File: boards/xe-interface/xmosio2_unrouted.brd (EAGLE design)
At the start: 116.8 x 55.2 mm, 105 parts, among them IC1 IDTQS3245QSOP20, IC2 IDTQS3245QSOP20, IC3 IDTQS3245QSOP20, IC4 IDTQS3245QSOP20, IC5 IDTQS3245QSOP20, U1 24 MHz Osc. (F535L-24), X1 0446200002

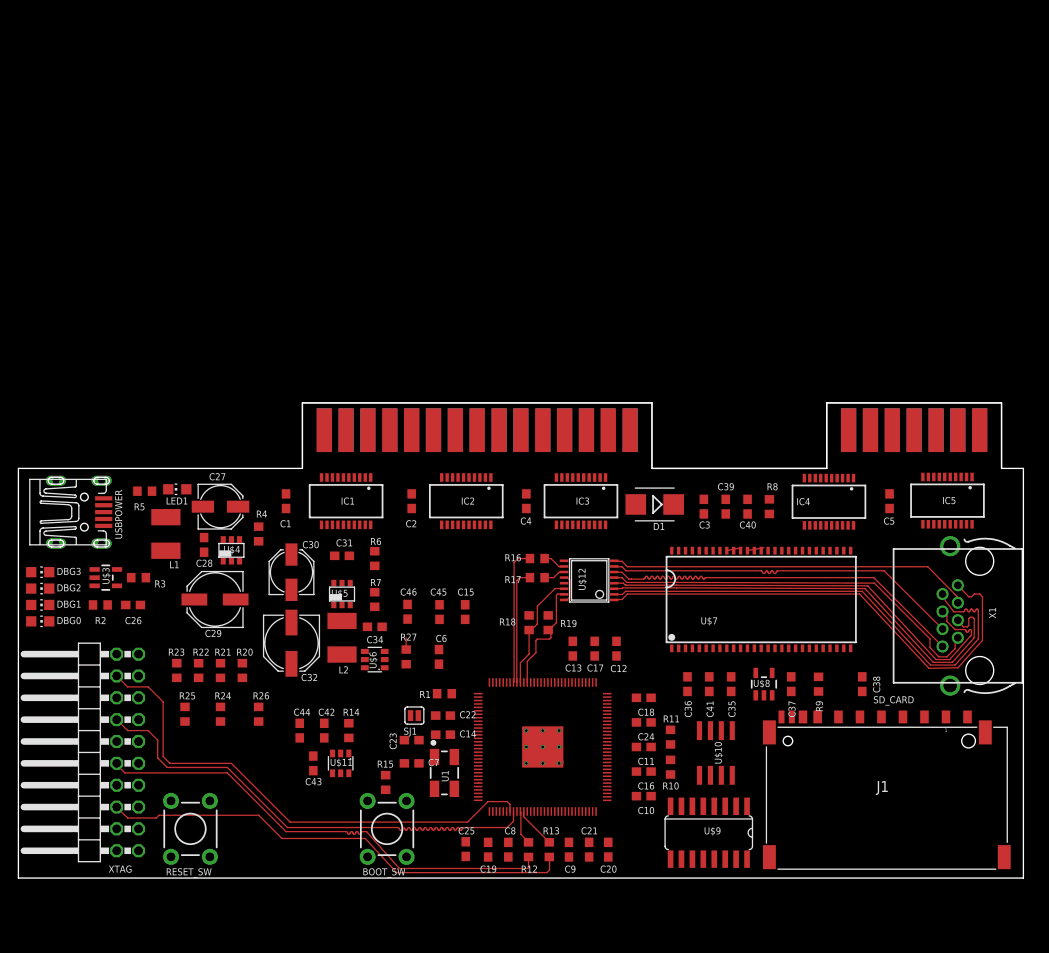
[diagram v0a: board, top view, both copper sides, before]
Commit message: Save the currently-unrouted-apart-from-high-speed-traces board in case something goes wrong
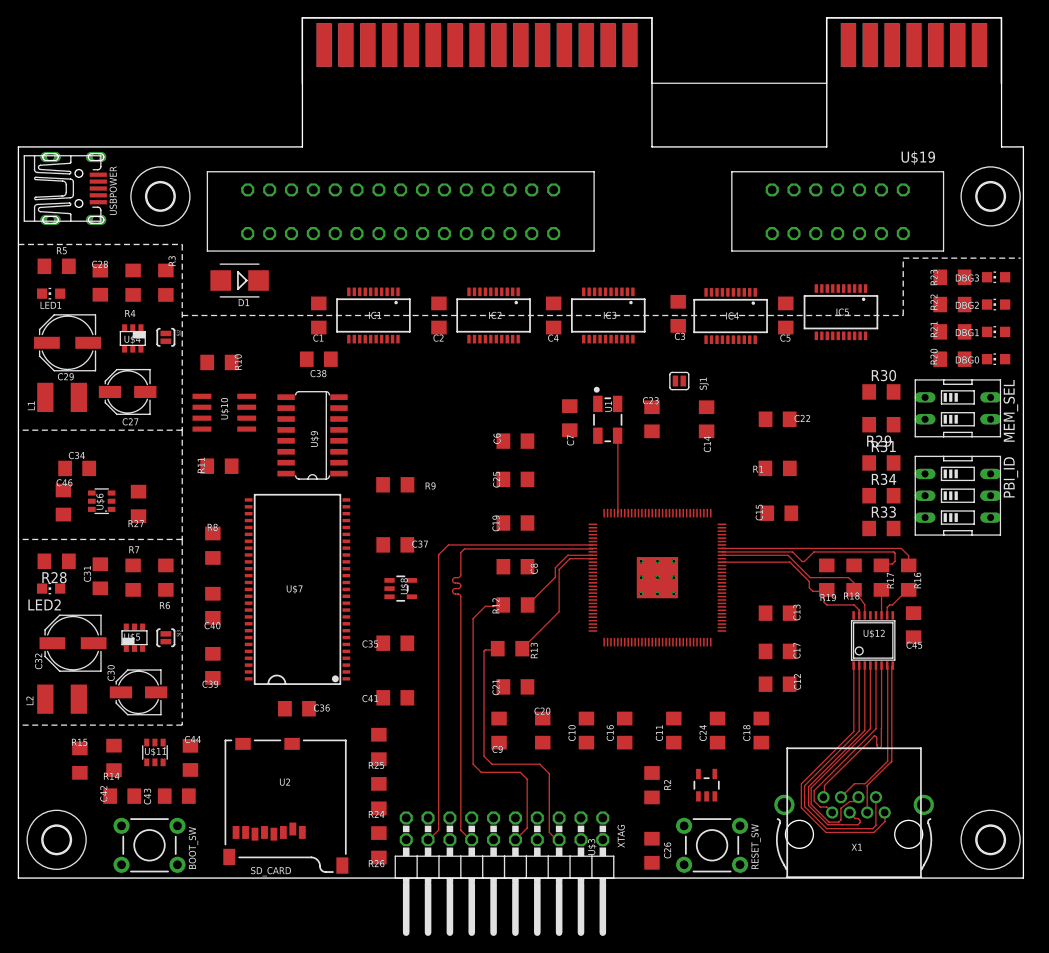
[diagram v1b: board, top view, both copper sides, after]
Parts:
- removed J1: (no value), InputOutputIO (rev17e):693063020911
- added H1, H2, H3, H4: MOUNT-HOLE3.2, holes:3,2
- added LED2: ok33, led:CHIP-LED0805
- added MEM_SEL: (no value), special:EDG-02
- added PBI_ID: (no value), special:EDG-03
- added R28: 47R, rcl:R1206
- added R29, R30, R31, R33, R34: 10K, rcl:R1206
- added SJ2, SJ3: SOLDERJUMPERNO, SparkFun:SJ_2S-NO
- added U$19: XE_SLOT, pbxl:XE_SLOT
- added U2: USD-SOCKETNEW, SparkFun-Connectors:MICRO-SD-SOCKET-PP
- C1, C10, C11, C12, C13, C14, C15, C16, C17, C18, C19, C2, C20, C21, C22, C23, C24, C25, C26, C28, C3, C31, C34, C35, C36, C37, C38, C39, C4, C40, C41, C42, C43, C44, C45, C46, C5, C6, C7, C8, C9: device rcl:C0603 -> rcl:C1206
- R1, R10, R11, R12, R13, R14, R15, R16, R17, R18, R19, R2, R20, R21, R22, R23, R24, R25, R26, R27, R3, R4, R5, R6, R7, R8, R9: device rcl:R0603 -> rcl:R1206
- moved DBG3 116.3 mm to (113.7, 69.8), turned to 90 degrees
- moved DBG2 115.9 mm to (113.7, 66.7), turned to 90 degrees
- moved DBG1 115.6 mm to (113.7, 63.5), turned to 90 degrees
- moved DBG0 115.2 mm to (113.7, 60.3), turned to 90 degrees
- moved R23 101.1 mm to (108.6, 69.8), turned to 180 degrees
- moved R22 97.4 mm to (108.6, 66.7), turned to 180 degrees
- moved R21 93.8 mm to (108.6, 63.5), turned to 180 degrees
- moved R20 90.1 mm to (108.6, 60.3), turned to 180 degrees
- moved U$3 73.9 mm to (80.0, 10.8), turned to 0 degrees
- moved C38 73.6 mm to (34.9, 60.3), turned to 180 degrees
- moved R10 70.5 mm to (23.4, 59.9), turned to 0 degrees
- moved U$10 69.5 mm to (23.9, 54.1), turned to 90 degrees
- moved R2 67.5 mm to (73.7, 10.8), turned to 90 degrees
- moved C26 66.8 mm to (73.7, 3.17), turned to 270 degrees
- moved U$9 65.2 mm to (34.2, 51.5), turned to 90 degrees
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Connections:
- removed net N$40: J1.CD
- removed net N$41: J1.WP
- new net N$30: C29.+, L1.1, LED1.A, R3.2, SJ2.1
- new net N$31: LED2.C, R28.2
- new net N$32: C32.+, L2.1, LED2.A, R6.2, SJ3.1
- new net N$34: MEM_SEL.2, R29.1, U$2.25
- new net N$35: MEM_SEL.1, R30.2, U$2.26
- new net PBI0: PBI_ID.1, R31.2, U$2.33
- new net PBI1: PBI_ID.2, R34.2, U$2.61
- new net PBI2: PBI_ID.3, R33.2, U$2.62
- net +5V: now also U$19.26, U$19.44
- net B1: now also U$19.1
- net B10: now also U$19.11
- net B11: now also U$19.12
- net B12: now also U$19.13
- net B13: now also U$19.14
- net B14: now also U$19.15
- net B15: now also U$19.16
- net B16: now also U$19.17
- net B17: now also U$19.18
- net B18: now also U$19.19
- net B19: now also U$19.20
- net B2: now also U$19.2
- net B20: now also U$19.21
- net B21: now also U$19.22
- net B22: now also U$19.23
- net B23: now also U$19.24
- net B24: now also U$19.25
- net B25: now also U$19.27
- net B26: now also U$19.28
- net B27: now also U$19.29
- net B28: now also U$19.30
- net B29: now also U$19.32
- net B3: now also U$19.4
- net B30: now also U$19.33
- net B31: now also U$19.34
- net B32: now also U$19.35
- net B33: now also U$19.36
- net B34: now also U$19.37
- net B35: now also U$19.38
- net B36: now also U$19.39
- net B37: now also U$19.41
- net B38: now also U$19.42
- net B4: now also U$19.5
- net B5: now also U$19.6
- net B6: now also U$19.7
- net B7: now also U$19.8
- net B8: now also U$19.9
- net B9: now also U$19.10
- net GND: now also R28.1, R29.2, R30.1, R31.1, R33.1, R34.1, U$19.3, U$19.43, U2.6, U2.CD1, U2.CD2, U2.GND1, U2.GND3; no longer J1.3, J1.6, J1.GND1, J1.GND2, J1.GND3, J1.GND4
- net SDC_CLK: now also U2.5; no longer J1.5
- net SDC_CMD: now also U2.3; no longer J1.2
- net SDC_D0: now also U2.7; no longer J1.7
- net SDC_D1: now also U2.8; no longer J1.8
- net SDC_D2: now also U2.1; no longer J1.9
- net SDC_D3: now also U2.2; no longer J1.1
- net VCCINT: now also SJ3.2; no longer C32.+, L2.1, R6.2, U$6.5
- net VCCIO: now also MEM_SEL.3, MEM_SEL.4, PBI_ID.4, PBI_ID.5, PBI_ID.6, SJ2.2, U$6.5, U2.4; no longer C29.+, J1.4, L1.1, LED1.A, R3.2
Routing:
- net RIN1_N: track 57.0 -> 31.6 mm
- net RIN1_P: track 57.0 -> 31.8 mm
- net JTAG_UP1: track 55.5 -> 30.7 mm
- net RIN2_N: track 52.1 -> 27.4 mm
- net RIN2_P: track 52.4 -> 27.9 mm
- net DOUT2_N: track 45.8 -> 21.4 mm
- net DOUT1_N: track 42.4 -> 18.3 mm
- net DOUT2_P: track 44.8 -> 20.9 mm
- net DOUT1_P: track 42.0 -> 18.3 mm
- net JTAG_UP0: track 55.3 -> 35.7 mm
- net N$23: track 4.82 -> 15.4 mm
- net N$28: track 13.5 -> 23.8 mm
- net N$2: track 0.28 -> 9.01 mm
- net LNK_IN1: track 13.6 -> 20.8 mm
- net N$29: track 16.0 -> 23.2 mm
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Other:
- board size 116.8 x 55.2 mm -> 116.8 x 100 mm

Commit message: Latest design changes  - Move the XTAG connector back significantly, so the shroud is not overhanging the board  - Use the SD card slot, not the micro-SD card, it’s easier to solder  - Fix the SD card pinouts  - Remove an unwanted pull-up on the SD card
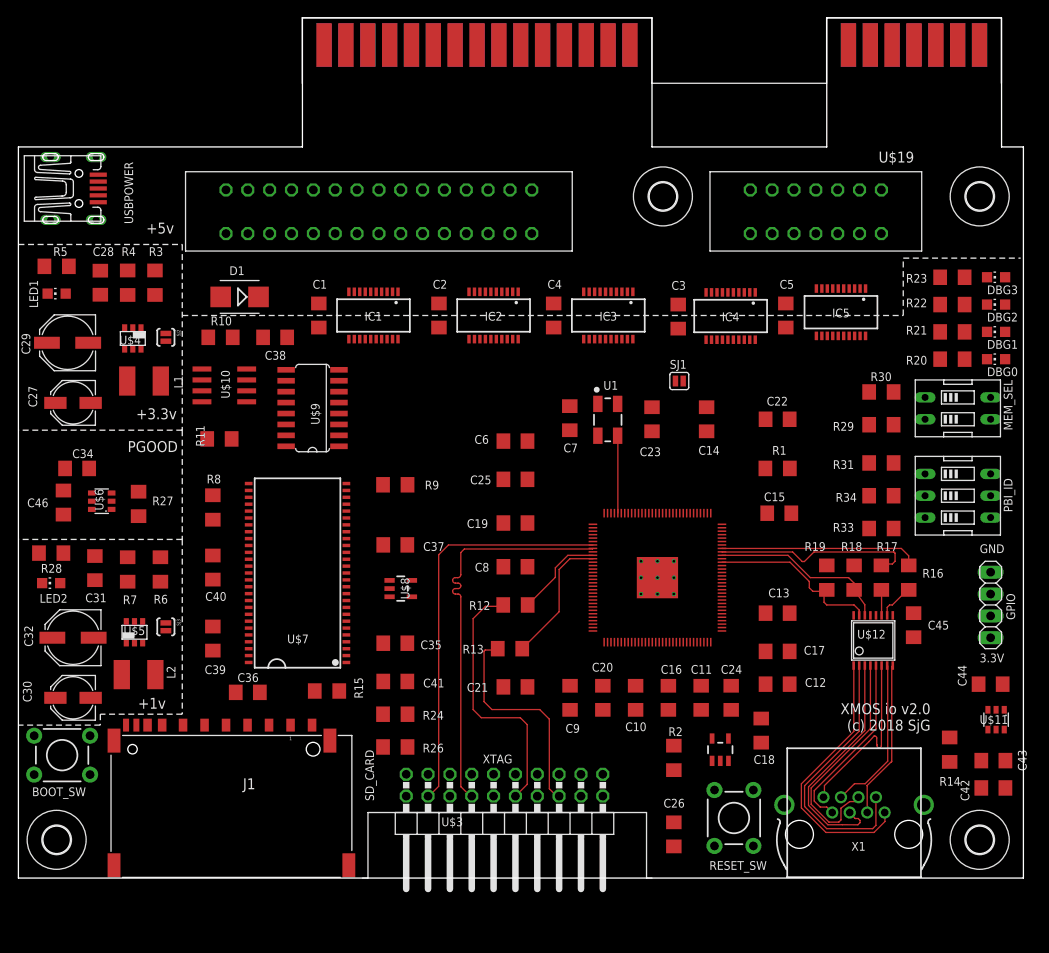
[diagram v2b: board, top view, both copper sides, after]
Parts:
- removed R25: 10K, rcl:R1206
- removed U2: USD-SOCKETNEW, SparkFun-Connectors:MICRO-SD-SOCKET-PP
- added GPIO: (no value), pinhead:1X04
- added J1: (no value), InputOutputIO (rev17e):693063020911
- moved C42 101.3 mm to (113.3, 10.5)
- moved U$11 97.9 mm to (113.7, 18.4)
- moved R14 97.2 mm to (108.3, 14.9)
- moved C43 95.0 mm to (113.3, 13.7)
- moved C44 93.4 mm to (113.0, 22.5), turned to 180 degrees
- moved H3 58.4 mm to (74.9, 79.2)
- moved R15 29.9 mm to (35.9, 21.7), turned to 180 degrees
- moved BOOT_SW 14.6 mm to (5.08, 14.3), turned to 180 degrees
- moved R26 11.6 mm to (43.8, 15.2), turned to 0 degrees
- moved R24 9.71 mm to (43.8, 19.1), turned to 180 degrees
- moved L1 9.71 mm to (14.6, 57.8), turned to 180 degrees
- moved L2 9.34 mm to (14.0, 23.7), turned to 180 degrees
- moved C9 9.09 mm to (64.1, 21.0)
- moved C20 7.96 mm to (67.9, 21.0), turned to 270 degrees
- moved C30 7.65 mm to (6.35, 21.0)
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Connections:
- new net N$36: GPIO.3, U$2.12
- new net N$37: GPIO.2, U$2.14
- new net SDC_CD: U$2.84
- net GND: now also GPIO.1, J1.3, J1.6, J1.GND1, J1.GND2, J1.GND3, J1.GND4; no longer R26.2, U2.6, U2.CD1, U2.CD2, U2.GND1, U2.GND3
- net SDC_CLK: now also U$2.64; no longer U$2.96, U2.5
- net SDC_CMD: now also U$2.63; no longer U$2.94, U2.3
- net SDC_D0: now also U$2.96; no longer R25.1, U$2.93, U2.7
- net SDC_D1: now also U$2.94; no longer U$2.92, U2.8
- net SDC_D2: now also U$2.93; no longer U$2.64, U2.1
- net SDC_D3: now also R26.2, U$2.92; no longer R26.1, U$2.63, U2.2
- net VCCIO: now also GPIO.4, R26.1; no longer R25.2, U2.4
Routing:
- net JTAG_DN0: track 51.9 -> 46.8 mm
- net JTAG_UP1: track 30.7 -> 25.6 mm
- net JTAG_DN1: track 52.1 -> 47.0 mm
- net JTAG_UP0: track 35.7 -> 30.6 mm
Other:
- board text added: "(c) 2018 SjG"
- board text added: "+1v"
- board text added: "+3.3v"
- board text added: "+5v"
- board text added: "3.3V"
- board text added: "GND"
- board text added: "PGOOD"
- board text added: "XMOS io v2.0"

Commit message: Update the routed and unrouted board files, delete an unwanted routed-board file
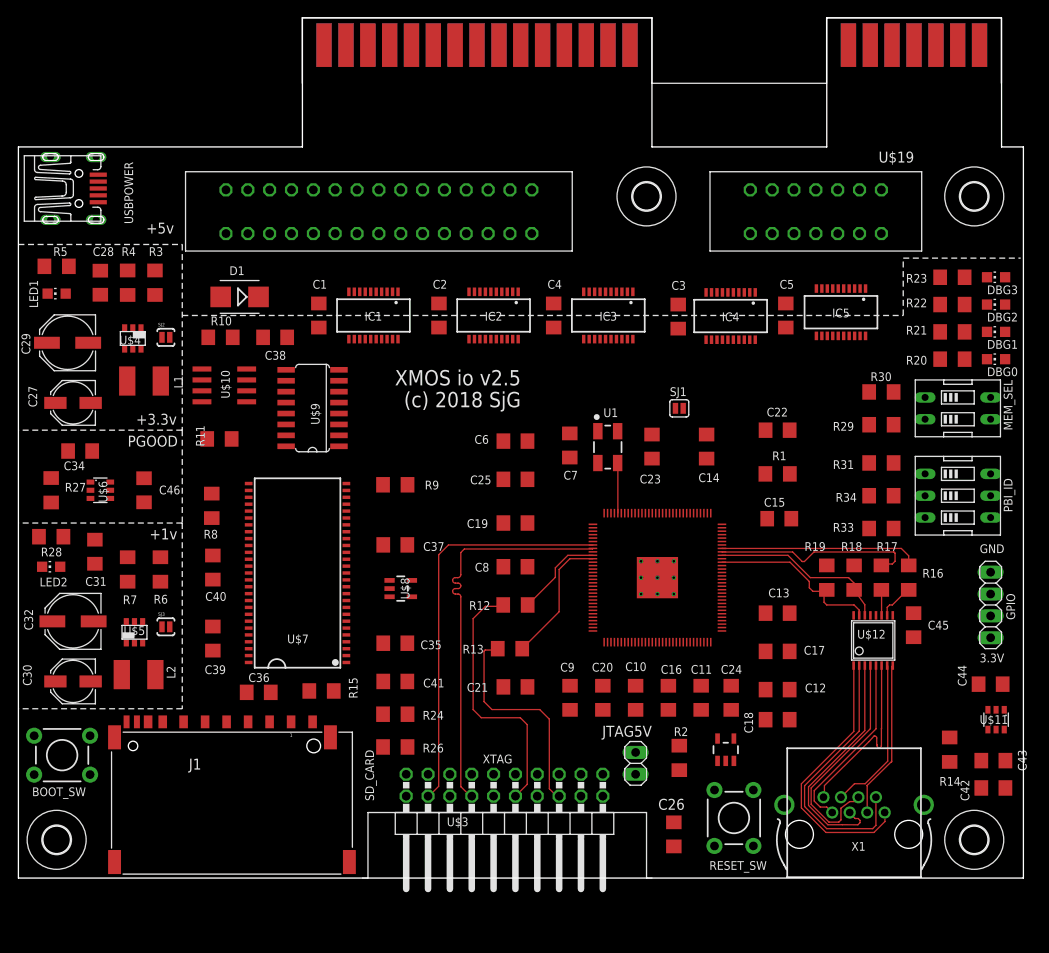
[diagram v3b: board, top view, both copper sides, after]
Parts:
- added JTAG5V: PSU, pinhead:1X02
- GPIO: value (none) -> UART
- J1: value (none) -> SD_CARD
- MEM_SEL: value (none) -> CT2092MS-ND
- PBI_ID: value (none) -> CT2093MS-ND
- moved R27 10.3 mm to (3.81, 45.1)
- moved C46 9.47 mm to (14.6, 45.1), turned to 270 degrees
- moved C14 3.18 mm to (80.0, 50.2)
- moved C23 3.18 mm to (73.7, 50.2)
- moved C7 3.17 mm to (64.1, 50.3)
- moved SJ1 3.17 mm to (76.8, 54.6)
- moved U1 3.17 mm to (68.5, 50.1)
- moved C18 2.29 mm to (88.3, 18.4), turned to 180 degrees
- moved C34 2.05 mm to (7.17, 49.6), turned to 0 degrees
- moved C30 1.91 mm to (6.35, 22.9)
- moved H3 1.91 mm to (73.0, 79.2)
- moved LED2 1.91 mm to (3.81, 36.2)
- moved R28 1.91 mm to (3.81, 39.7)
- moved C32 1.90 mm to (6.35, 29.8)
- moved C31 1.90 mm to (8.89, 37.9)
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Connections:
- net N$21 renamed TRST_N
- removed net N$36: GPIO.3, U$2.12
- removed net N$37: GPIO.2, U$2.14
- new net N$38: JTAG5V.2, XTAG.1
- new net UART_RX: GPIO.2, U$2.14, XTAG.19
- new net UART_TX: GPIO.3, U$2.12, XTAG.17
- net +5V: now also JTAG5V.1
- net SDC_CD: now also J1.CD
- net SDC_CLK: now also J1.5
- net SDC_CMD: now also J1.2
- net SDC_D0: now also J1.7
- net SDC_D1: now also J1.8
- net SDC_D2: now also J1.9
- net SDC_D3: now also J1.1
- net VCCIO: now also J1.4
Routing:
- net N$2: track 9.01 -> 5.84 mm
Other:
- board text added: "XMOS io v2.5"
- board text removed: "XMOS io v2.0"

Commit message: Latest board files. Submitted board is xmosio2_routed.brd
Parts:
- removed D1: MURS120-E3, diode:SMB
- added D2: (no value), SparkFun-DiscreteSemi:DIODE-1N4001-KIT
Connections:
- net +4.3V: now also D2.C; no longer D1.C
- net +5V: now also D2.A; no longer D1.A
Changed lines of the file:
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@@
 <setting verticaltext="up"/>
 </settings>
-<grid distance="0.025" unitdist="inch" unit="inch" style="lines" multiple="1" display="no" altdistance="0.025" altunitdist="inch" altunit="inch"/>
+<grid distance="0.0125" unitdist="inch" unit="inch" style="lines" multiple="1" display="no" altdistance="0.025" altunitdist="inch" altunit="inch"/>
 <layers>
 <layer number="1" name="Top" color="4" fill="1" visible="yes" active="yes"/>
@@
 <attribute name="VALUE" x="64.77" y="64.135" size="1.27" layer="27" rot="R90"/>
 </element>
-<element name="D1" library="diode" package="SMB" value="MURS120-E3" x="25.7175" y="67.564" smashed="yes" rot="R180">
-<attribute name="NAME" x="26.289" y="71.12" size="1.016" layer="25" rot="R180"/>
-<attribute name="VALUE" x="27.8765" y="70.993" size="1.27" layer="27" rot="R180"/>
-</element>
 <element name="U$2" library="Eagle_XMOS_Lib_COMPLETE" package="TQFP128" value="XL216-512-TQ128" x="74.295" y="34.925" smashed="yes"/>
 <element name="C6" library="rcl" package="C1206" value="100nF" x="57.785" y="50.8" smashed="yes" rot="R180">
@@
 <attribute name="VALUE" x="68.58" y="15.875" size="1.27" layer="27" rot="R270"/>
 </element>
+<element name="D2" library="SparkFun-DiscreteSemi" package="DIODE-1N4001-KIT" value="" x="26.035" y="67.945"/>
 </elements>
 <signals>
@@
 </signal>
 <signal name="+5V" class="1">
-<contactref element="D1" pad="A"/>
 <contactref element="U$4" pad="3"/>
 <contactref element="C27" pad="+"/>
@@
 <contactref element="U$19" pad="26"/>
 <contactref element="JTAG5V" pad="1"/>
+<contactref element="D2" pad="A"/>
 <wire x1="100.33" y1="80.01" x2="111.74" y2="96.845" width="0" layer="19" extent="16-16"/>
 <wire x1="66.02" y1="96.845" x2="100.33" y2="80.01" width="0" layer="19" extent="16-16"/>
 <wire x1="54.61" y1="80.01" x2="66.02" y2="96.845" width="0" layer="19" extent="16-16"/>
-<wire x1="23.5175" y1="67.564" x2="54.61" y2="80.01" width="0" layer="19" extent="1-1"/>
-<wire x1="12.35045625" y1="63.9839375" x2="23.5175" y2="67.564" width="0" layer="19" extent="1-1"/>
+<wire x1="20.955" y1="67.945" x2="54.61" y2="80.01" width="0" layer="19" extent="1-1"/>
+<wire x1="12.35045625" y1="63.9839375" x2="20.955" y2="67.945" width="0" layer="19" extent="1-1"/>
 <wire x1="13.30045625" y1="61.4839375" x2="12.35045625" y2="63.9839375" width="0" layer="19" extent="1-1"/>
 <wire x1="4.3" y1="55.245" x2="13.30045625" y2="61.4839375" width="0" layer="19" extent="1-1"/>
@@
 </signal>
 <signal name="+4.3V">
-<contactref element="D1" pad="C"/>
 <contactref element="C2" pad="1"/>
 <contactref element="IC1" pad="20"/>
@@
 <contactref element="C4" pad="1"/>
 <contactref element="IC5" pad="20"/>
+<contactref element="D2" pad="C"/>
 <wire x1="89.2175" y1="64.005" x2="98.489" y2="63.036" width="0" layer="19" extent="1-1"/>
 <wire x1="85.662" y1="62.5915" x2="89.2175" y2="64.005" width="0" layer="19" extent="1-1"/>
@@
 <wire x1="44.133" y1="62.655" x2="48.895" y2="64.005" width="0" layer="19" extent="1-1"/>
 <wire x1="34.925" y1="64.005" x2="44.133" y2="62.655" width="0" layer="19" extent="1-1"/>
-<wire x1="27.9175" y1="67.564" x2="34.925" y2="64.005" width="0" layer="19" extent="1-1"/>
+<wire x1="31.115" y1="67.945" x2="34.925" y2="64.005" width="0" layer="19" extent="1-1"/>
 </signal>
 <signal name="N$10">
